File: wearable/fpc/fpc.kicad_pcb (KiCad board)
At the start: 2 copper layers, 22.4 x 21 mm, 3 parts, among them J1 FPC, J2 FPC

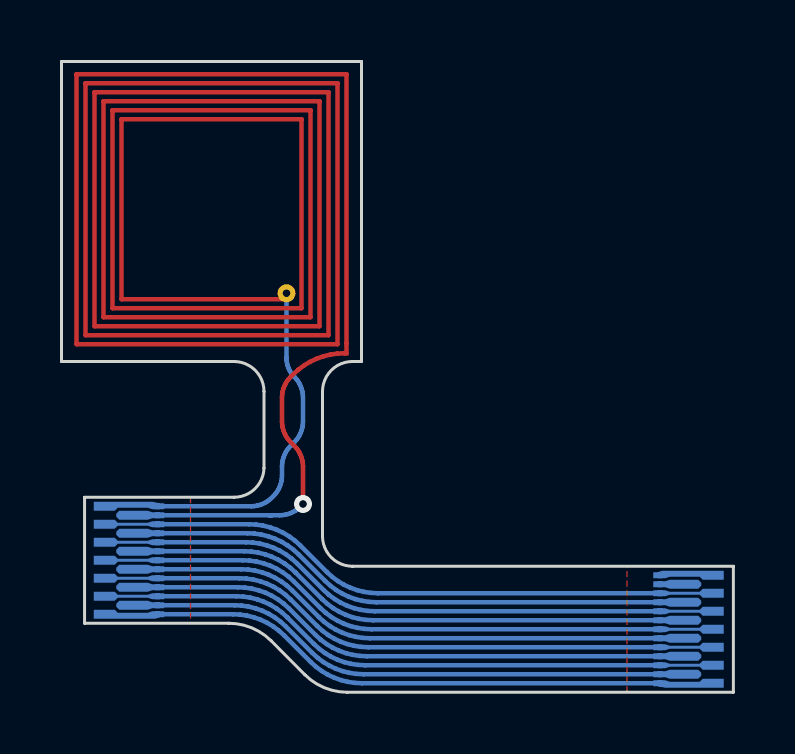
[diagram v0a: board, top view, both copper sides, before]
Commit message: Review the wearable ribbon cable for manufacturing.
- Do teardrops at vias.
- Make it up with logo & copyright text.

Signed-off-by: Mike M. Volokhov <mike.volokhov@gmail.com>
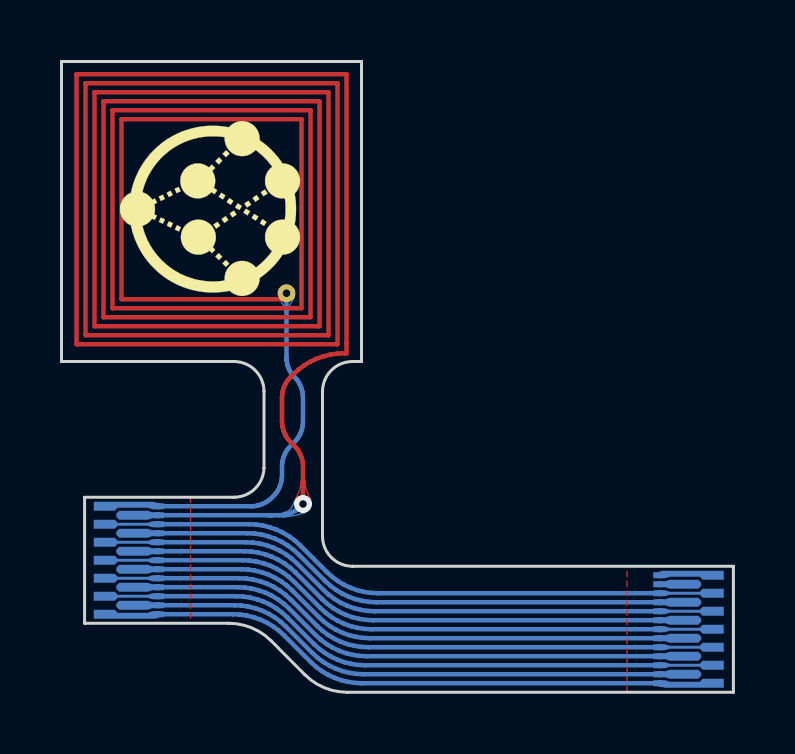
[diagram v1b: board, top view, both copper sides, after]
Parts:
- added G***: LOGO, Herald_Wearable_FPC:Herald_Logo_6x6mm_Silk, F.Cu at (154.2, 86.4)
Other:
- board text added: "Some text here © 2021 Herald"
